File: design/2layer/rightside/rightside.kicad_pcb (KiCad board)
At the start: 2 copper layers, 142.6 x 98.8 mm, 211 parts, among them IC1 XCL240B333FR-G, IC3 nRF52833-QDAA-R7, IC4 TCA9537DGSR, IC5 XCL110A503KR-G, IC6 TPS22917LDBVT, IC7 SN74AHCT1G125DCKR, J1 USB_C_Receptacle_USB2.0_16P, J2 Battery+, J3 Battery-, J4 OLED_128x32, J6 Conn_01x04, J7 F32Q-1A7H1-11012, U1 BQ27441-G1, U2 BQ24072RGT, U3 USB6B1, U5 PEC11L-4015F-S0015, Y1 ECS-320-8-37B2-JTY-TR

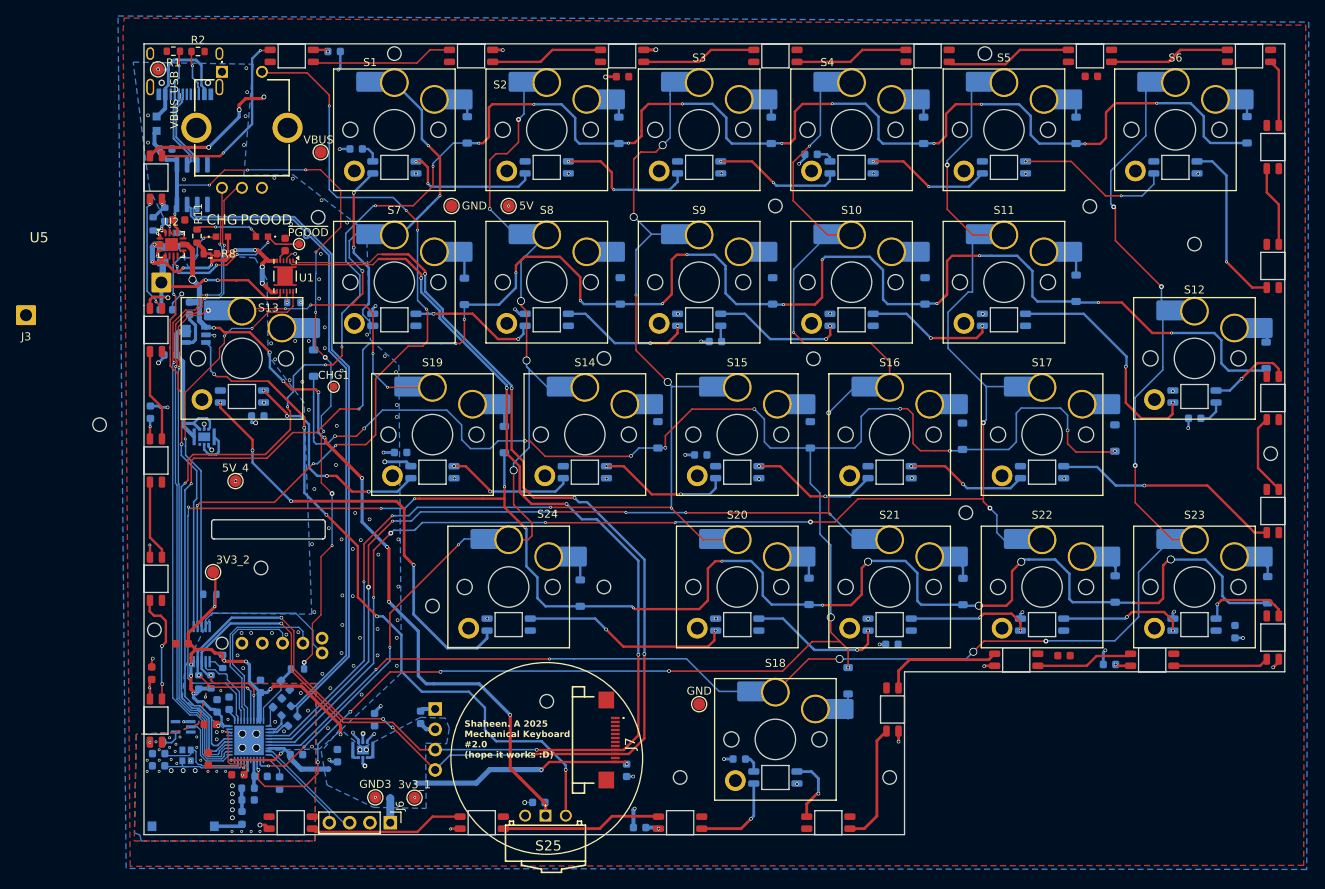
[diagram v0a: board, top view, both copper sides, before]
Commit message: begin better, more systematic 2 layer wiring
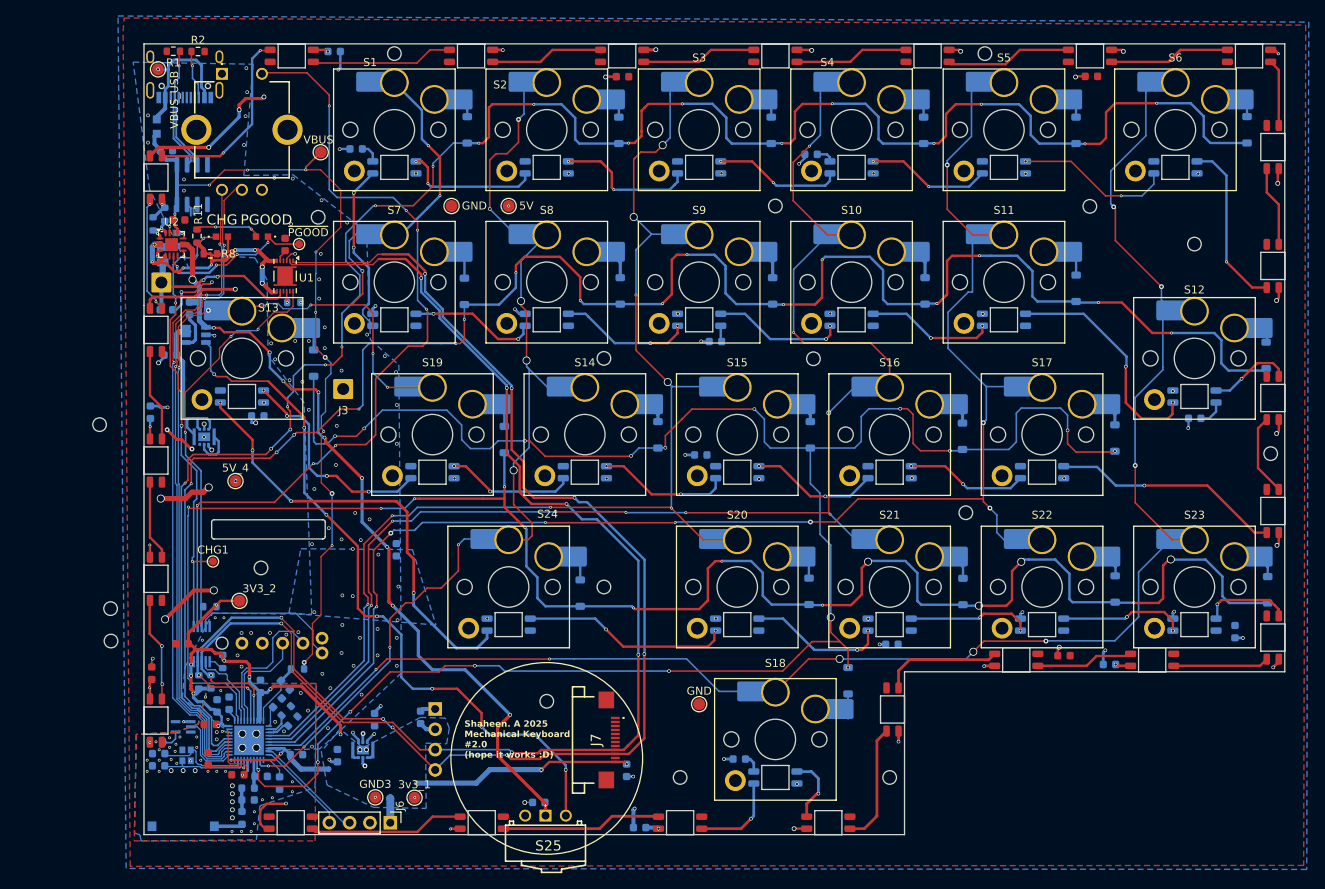
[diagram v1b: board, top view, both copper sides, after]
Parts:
- moved J3 40.7 mm to (43.5, 57.6)
- moved REF** 40.4 mm to (14.4, 89.1)
- moved CHG1 26.5 mm to (27.2, 79.2)
- moved C41 12.2 mm to (50.1, 77.7), turned to 90 degrees
- moved U5 7.67 mm to (30.8, 25.2)
- moved REF** 6.08 mm to (14.4, 85.1)
- moved 3V3_2 4.88 mm to (30.5, 84.1)
- moved R12 1.54 mm to (26.8, 84.8)
- moved J1 0.40 mm to (23.7, 17.1)
- moved F1 0.36 mm to (20.2, 24.8)
- moved C24 0.20 mm to (21.4, 27.8)
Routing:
- net D+: track 82.1 -> 1.46 mm
- net D-: track 82.1 -> 1.60 mm
- net 5V: track 63.5 -> 109.9 mm, vias 23 -> 39
- net /CCW2: track 20.0 -> 14.5 mm
- net /CW2: track 22.7 -> 18.4 mm
- net GND: track 50.3 -> 54.3 mm, vias 172 -> 180
- net Net-(Di3-A): track 0.00 -> 3.79 mm
- net Net-(Di13-A): track 0.00 -> 3.79 mm
- net Net-(Di12-A): track 0.00 -> 3.79 mm
- net 3V3: track 111.5 -> 108.3 mm
- net Net-(Di5-A): track 0.00 -> 3.10 mm
- net Net-(Di18-A): track 0.00 -> 2.88 mm
- net Net-(Di17-A): track 0.00 -> 2.71 mm
- net Net-(Di16-A): track 0.00 -> 2.71 mm
- net /CHG: track 56.0 -> 58.7 mm, vias 4 -> 5
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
